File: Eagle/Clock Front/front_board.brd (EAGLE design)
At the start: 14 parts

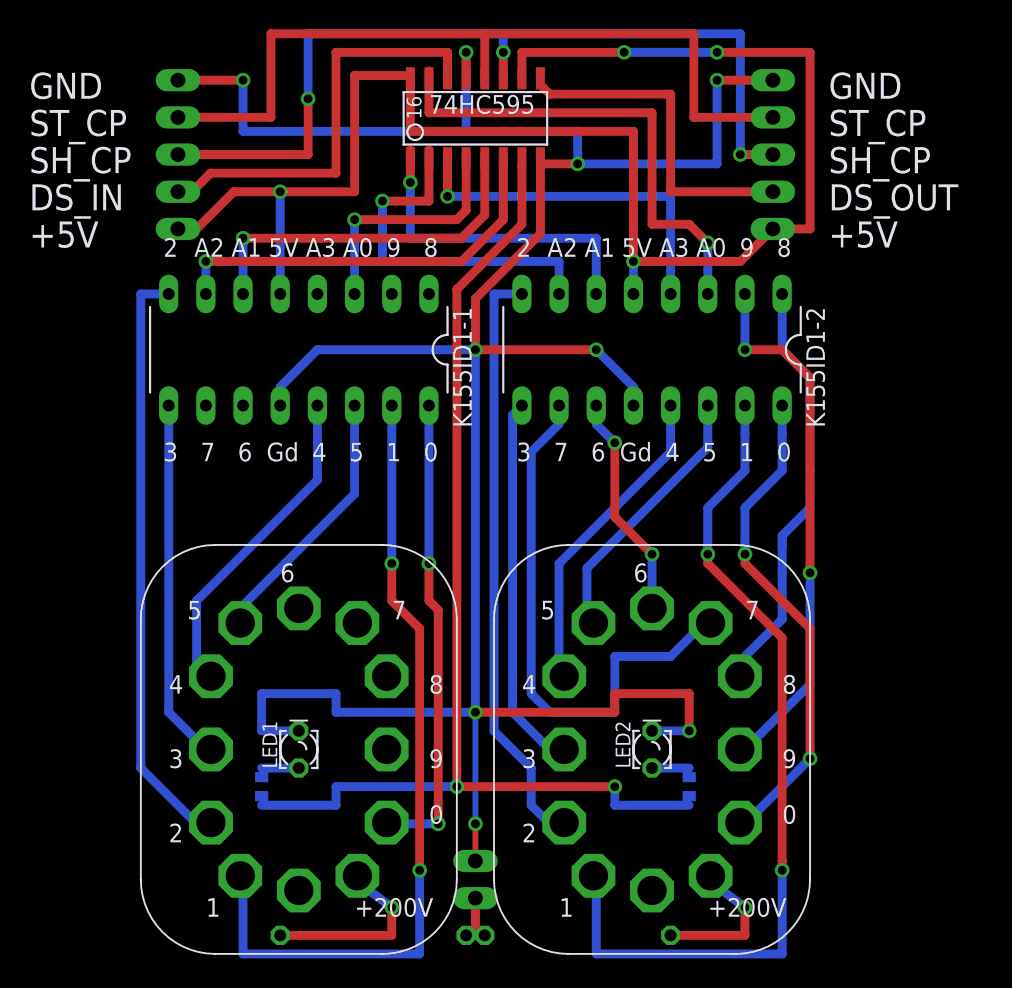
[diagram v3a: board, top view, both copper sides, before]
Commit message: Обновление печатной платы для цоколей. Компактизация
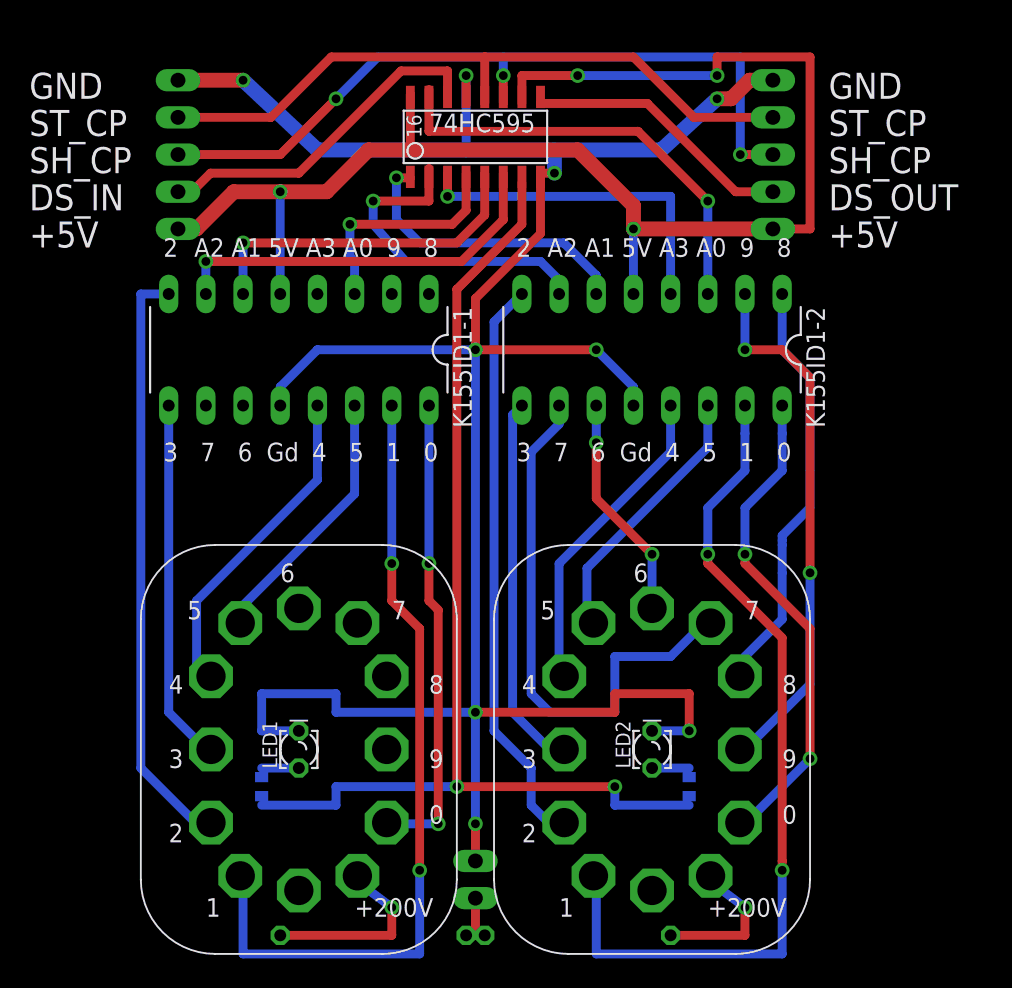
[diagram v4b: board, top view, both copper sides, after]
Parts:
- moved 74HC595 1.27 mm to (0.00, 29.2)
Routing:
- net +5V: track 109.0 -> 98.4 mm
- net GND: track 182.4 -> 173.4 mm
- net ST_CP: track 55.6 -> 47.2 mm
- net SH_CP: track 60.6 -> 53.2 mm
- net DATA_IN: track 29.1 -> 23.7 mm
- net DATA_OUT: track 22.8 -> 18.4 mm
- net S$23: track 33.5 -> 30.2 mm
- net S$26: track 22.5 -> 20.3 mm
- net S$25: track 25.1 -> 23.0 mm
- net S$20: track 25.1 -> 23.6 mm
- net S$9: track 28.2 -> 26.9 mm
- net S$24: track 24.8 -> 23.5 mm
- net LED+: track 76.1 -> 74.9 mm
- net S$5: track 40.3 -> 39.2 mm
- net S$21: track 16.8 -> 15.8 mm

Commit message: Обновление печатной платы для цоколей. Мелкое улучшательство.
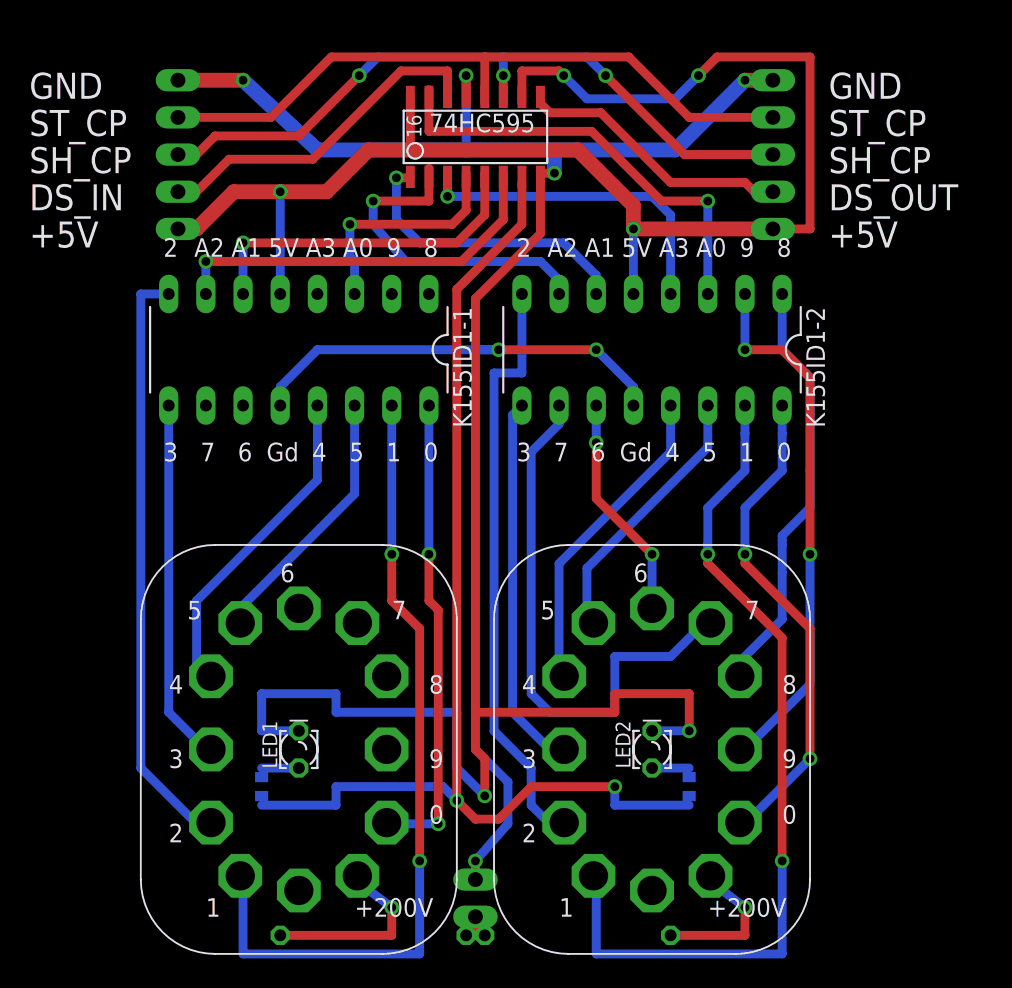
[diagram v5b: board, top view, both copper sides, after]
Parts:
- moved 200VCONNECTOR 1.27 mm to (0.00, -22.9)
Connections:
- removed net GND: IN.5, K155ID1-1.12, K155ID1-2.12, LED1.K, LED2.K
- new net GND_HIGH: K155ID1-1.12, K155ID1-2.12
- new net GND_LOW: IN.5, LED1.K, LED2.K
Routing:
- net GND: track 173.4 -> 0.00 mm, vias 9 -> 0
- net GND_LOW: track 0.00 -> 145.8 mm, vias 0 -> 6
- net GND_HIGH: track 0.00 -> 68.3 mm, vias 0 -> 3
- net SH_CP: track 53.2 -> 49.3 mm
- net LED+: track 74.9 -> 77.7 mm
- net +200V: track 3.81 -> 2.54 mm
- net S$5: track 39.2 -> 40.3 mm
- net +5V: track 98.4 -> 99.4 mm
- net S$24: track 23.5 -> 22.8 mm

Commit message: Обновление печатной платы для цоколей. Мелкое улучшательство.
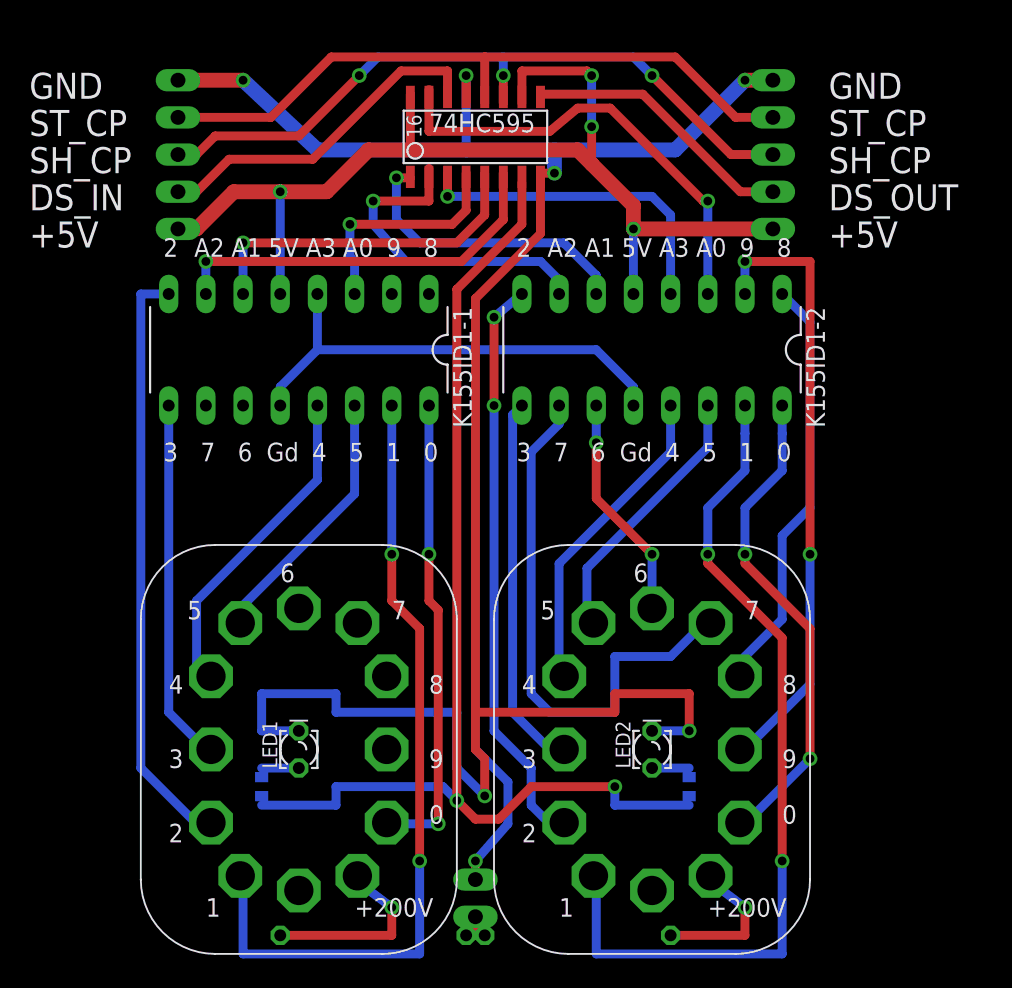
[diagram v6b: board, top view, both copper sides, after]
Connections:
- net GND_HIGH: now also K155ID1-1.4
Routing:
- net +5V: track 99.4 -> 74.4 mm
- net S$2: track 36.3 -> 41.8 mm
- net GND_HIGH: track 68.3 -> 70.5 mm, vias 3 -> 1
- net S$23: track 30.2 -> 31.5 mm
- net S$5: track 40.3 -> 39.3 mm, vias 0 -> 2

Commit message: Обновление печатной платы для цоколей. Еще мелкие улучшения. Контакт A3 К155ИД1-1 теперь подвязан к низковольтной земле.
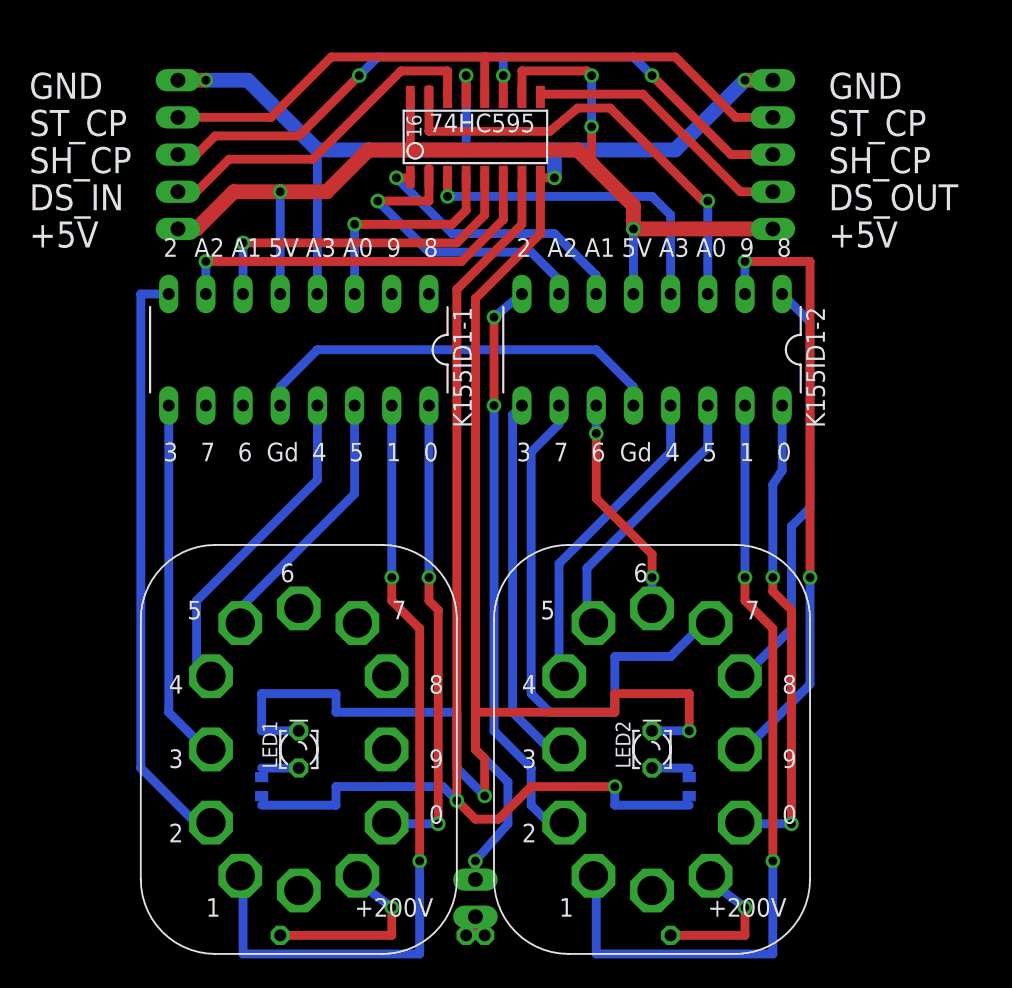
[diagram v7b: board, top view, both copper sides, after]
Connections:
- net GND_HIGH: no longer K155ID1-1.4
- net GND_LOW: now also K155ID1-1.4
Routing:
- net GND_LOW: track 145.8 -> 155.7 mm
- net GND_HIGH: track 70.5 -> 66.7 mm
- net S$12: track 34.3 -> 31.9 mm
- net S$26: track 20.3 -> 18.6 mm
- net S$25: track 23.0 -> 21.3 mm
- net S$3: track 33.3 -> 32.5 mm
- net S$13: track 24.1 -> 23.5 mm
